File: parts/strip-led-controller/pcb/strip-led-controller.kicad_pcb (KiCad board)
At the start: 2 copper layers, 100 x 48 mm, 17 parts, among them J1 BUCK_IN, J2 PWR IN, J3 BUCK_OUT, SW2 SW_SPDT, U1 ESP32 Wemos D1 Mini

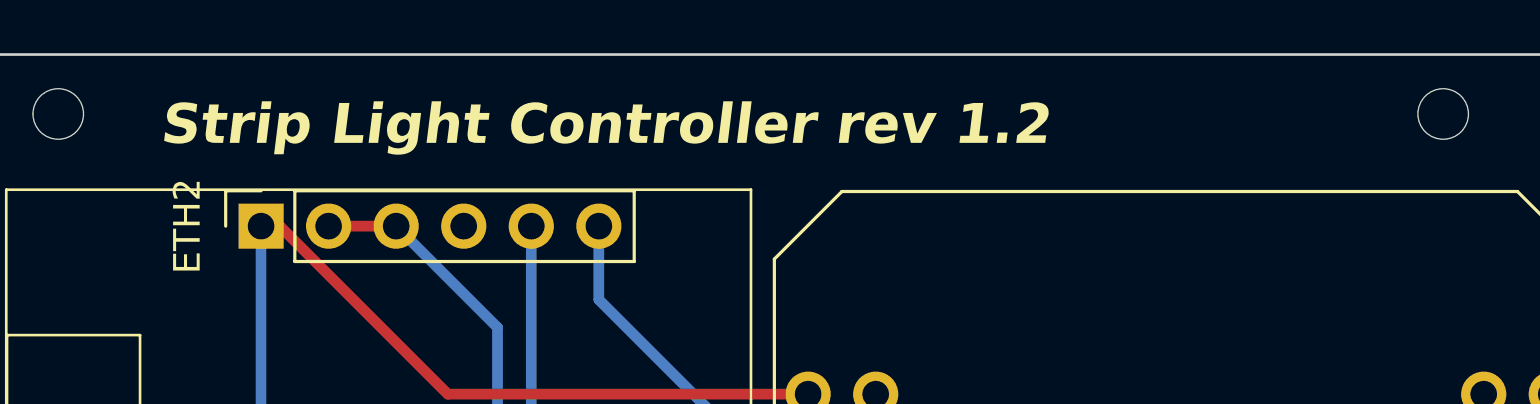
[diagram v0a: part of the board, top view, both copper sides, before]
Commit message: update QR code.
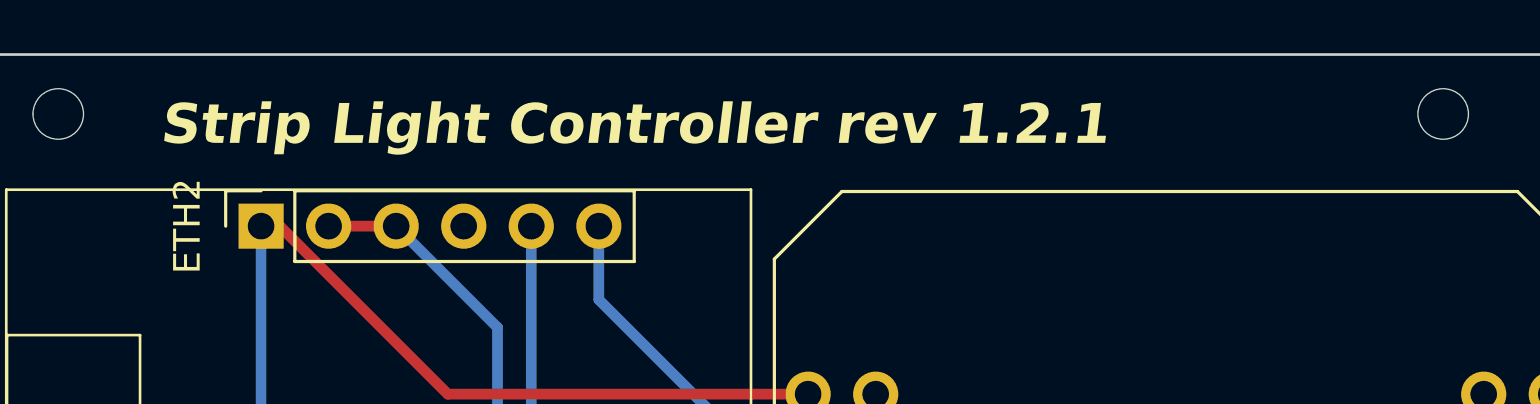
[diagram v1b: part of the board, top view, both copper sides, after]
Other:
- board text added: "Strip Light Controller rev 1.2.1"
- board text removed: "Strip Light Controller rev 1.2"
